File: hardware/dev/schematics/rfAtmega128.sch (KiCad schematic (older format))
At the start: 6 parts

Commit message: New schematic to finish at home.
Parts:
- added C?: 330n, symbol CAP_0603
- added C?: 22u, symbol CAP_0603
- added C? (x14): 100n, symbol CAP_0603
- added C?: 4.7u, symbol CAP_0603
- added J?: TEST_VDD33, symbol TEST_PAD
- added J?: TEST_GND, symbol TEST_PAD
- added J? (x2): J2PIN, symbol J2PIN
- added J?: PWR_ON/OFF, symbol J2PIN
- added R? (x12): RES_0603, symbol RES_0603
- added U?: FT232RL, symbol FT232RL
- added U?: LED_RED, symbol LED_RED
- added U? (x2): LED_GREEN, symbol LED_GREEN
- added U?: Q16.000, symbol Q16.000
- added XT?: FTDI_CONN, symbol FTDI_CONN
- gave numbers to parts that had none: 1
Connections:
- net GND: now reaches U?.11 (TEST)
- net GND: now also U?.1, U?.10 (AVSS_RFN), U?.20 (DVSS:DSVSS), U?.24 (DVSS), U?.35 (DVSS), U?.45 (DVSS), U?.55 (DVSS), U?.58 (AVSS:AVSS), U?.6 (GND), U?.61 (AVSS), U?.65 (AVSS_PAD), U?.7 (AVSS_RFP), XT?.4 (GND), XT?.5 (Shield), XT?.6 (Shield), C?.2, C?.2, C?.2, C?.2, C?.2, C?.2, C?.2, C?.2, C?.2, C?.2, C?.2, C?.2, C?.2, C?.2, C?.2, C?.2, J?.1, R?.2, U?.18 (GND), U?.2 (K), U?.21 (GND), U?.25 (AGND), U?.26 (TEST), U?.7 (GND), XT?.16
- net RESET: now reaches U?.12 (RESET)
- net RESET: now also C?.2, R?.1, R?.2
- net pwr_atmega: now reaches U?.33 (CLKI)
- net pwr_atmega: now also U?.21 (DVDD), U?.22 (DVDD), U?.23 (DEVDD), U?.34 (DEVDD), U?.44 (DEVDD), U?.54 (DEVDD), U?.59 (EVDD), C?.1, C?.1, C?.1, C?.1, C?.1, J?.2, R?.2
- net at U?.56 (XTAL2): now also C?.1, R?.2, U?.1
- net at U?.57 (XTAL1): now also C?.1, R?.1, U?.3
- net at U?.60 (AVDD): now also C?.1
- net aref: now reaches U?.62 (AREF)
- net aref: now also C?.1
- net at XT?.1 (VCC): now also U?.1 (A)
- net DM: now reaches XT?.2 (DM)
- net DM: now also R?.2
- net DP: now reaches XT?.3 (DP)
- net DP: now also R?.2
- net at U?.2 (K): now also U?.2 (VCC), C?.1, J?.1
- net at U?.1 (CTL): now also J?.2, R?.1
- net vdd33: now reaches U?.4 (OUT)
- net vdd33: now also C?.1, J?.1, J?.1, J?.1, R?.1
- net at U?.3: now also R?.1
- new net: R?.1, U?.15 (USBDP)
- new net: R?.1, U?.16 (USBDM)
- new net: C?.1, C?.1, U?.17 (3V3OUT), U?.4 (VCCIO)
- new net: C?.1, U?.19 (RESET#)
- new net: R?.2, U?.1 (A)
- new net: R?.1, U?.1 (A) (x2)
- new net CBUS0_CONN: U?.2 (K), U?.23 (CBUS0), XT?.11
- new net CBUS1_CONN: U?.2 (K), U?.22 (CBUS1), XT?.12
- new net CBUS2_CONN: U?.13 (CBUS2), XT?.13
- new net CBUS3_CONN: U?.14 (CBUS3), XT?.14
- new net CBUS4_CONN: U?.12 (CBUS4), XT?.15
- new net CTS_CONN: U?.11 (CTS#), XT?.6
- new net DCD_CONN: U?.10 (DCD#), XT?.9
- new net DSR_CONN: U?.9 (DSR#), XT?.8
- new net DTR_CONN: C?.1, U?.2 (DTR#), XT?.7
- new net RI_CONN: U?.6 (RI#), XT?.10
- new net RTS_CONN: R?.1, U?.3 (RTS#), XT?.5
- new net RXD: R?.2
- new net RXD_CONN: R?.1, U?.5 (RXD), XT?.4
- new net TXD: R?.2
- new net TXD_CONN: R?.1, U?.1 (TXD), XT?.3
- new net pwr_ftdi: C?.1, C?.1, J?.2, R?.2, R?.2, U?.20 (VCC)
- no-connect marks 0 -> 9
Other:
- note added: "FTDI Chip connector\nContains all FTDI pins on a 2x7 pins connector\nPins are 3.3V level internal connected"
- note added: "FTDI\nAll signals are lead to XT connector.\nRXD and TXD pins are flipped and lead to ATmega128rfA1"
- note added: "POWER SUPPLY \nInput: 4.0 - 32.0 VDC\nOutput: 3.3 VDC"
- moved on the sheet: U?, U?A, U?B, XT?

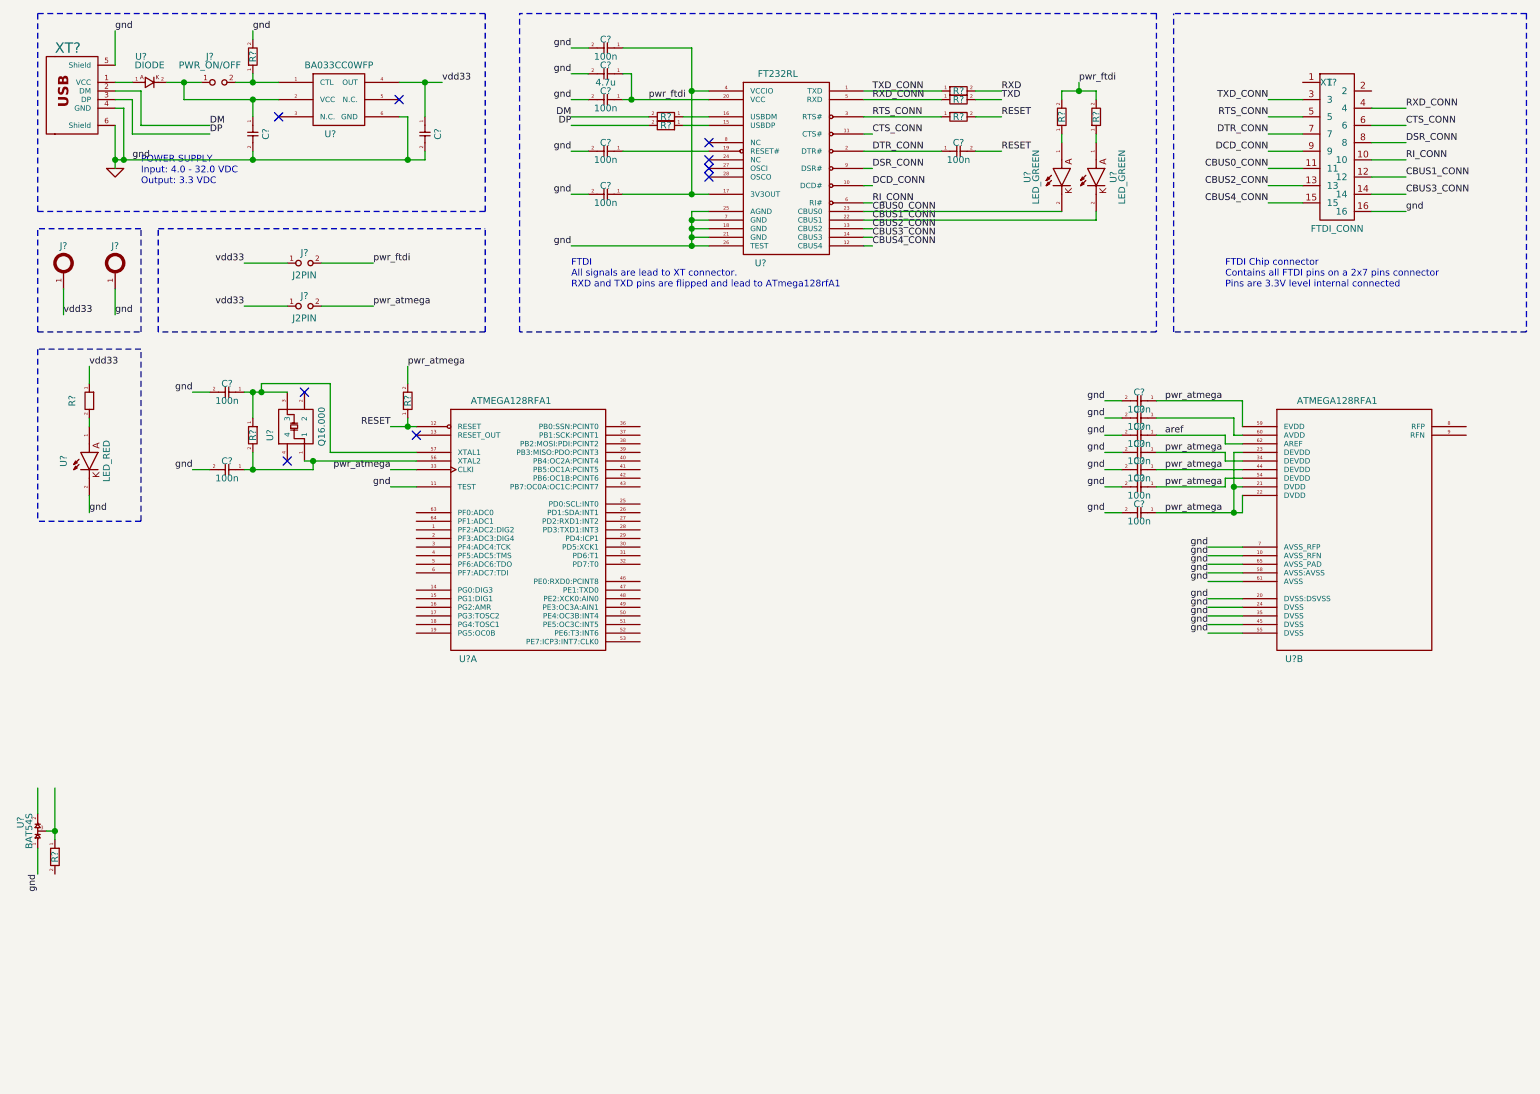
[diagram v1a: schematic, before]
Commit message: dev board schematic is finished now. Need to add modules of few resistors and condensators.
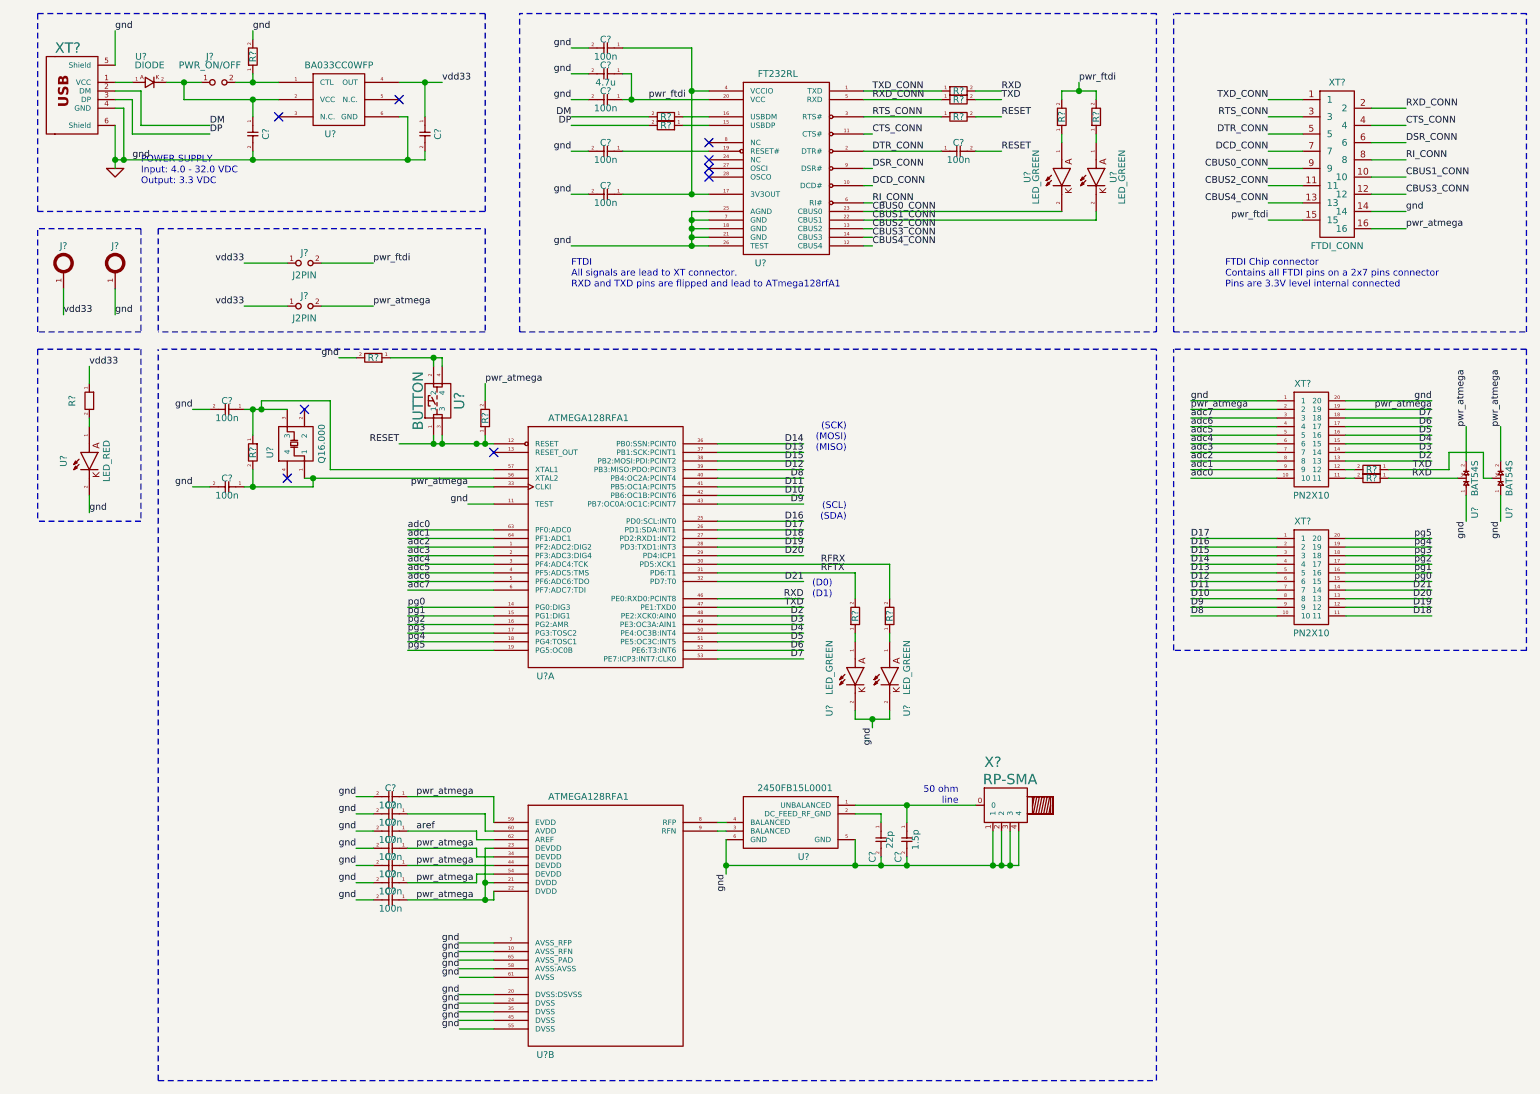
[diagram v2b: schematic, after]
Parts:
- removed R?: RES_0603, symbol RES_0603
- added C?: 22p, symbol CAP_0603
- added C?: 1.5p, symbol CAP_0603
- added R? (x4): RES_0603, symbol RES_0603
- added R?: 51, r_0603, symbol RES_0603
- added U?: BAT54S, SOT23EBC, symbol BAT54S
- added U? (x2): LED_GREEN, KP-2012ZGC, symbol LED_GREEN
- added U?: 2450FB15L0001, 2450FB15L0001, symbol 2450FB15L0001
- added U?: BUTTON, symbol BUTTON
- added X?: RP-SMA, rp-sma, symbol RP-SMA
- added XT? (x2): PN2X10, symbol PN2X10
- C? (x6): footprint (none) -> c_0603
- C? (x2): footprint (none) -> c_0805
- J? (x2): footprint (none) -> testpoint_2mm5
- R? (x3): value RES_0603 -> 2.7K; footprint (none) -> r_0603
- R? (x5): value RES_0603 -> 510; footprint (none) -> r_0603
- R?: value RES_0603 -> 100K; footprint (none) -> r_0603
- R?: footprint (none) -> r_0603
- U? (x2): footprint (none) -> atmega128rfa1
- U?: footprint (none) -> melf
- U?: footprint (none) -> BA033CCOWFP
- U?: footprint (none) -> SOT23EBC
- U?: footprint (none) -> SSOP28
- U? (x3): footprint (none) -> KP-2012ZGC
- U?: footprint (none) -> crystal_xg6x3p5
- XT?: footprint (none) -> USB_B
- XT?: footprint (none) -> BH16R
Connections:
- net CBUS0_CONN: now also XT?.9; no longer XT?.11
- net CBUS1_CONN: now also XT?.10; no longer XT?.12
- net CBUS2_CONN: now also XT?.11; no longer XT?.13
- net CBUS3_CONN: now also XT?.12; no longer XT?.14
- net CBUS4_CONN: now also XT?.13; no longer XT?.15
- net CTS_CONN: now also XT?.4; no longer XT?.6
- net DCD_CONN: now also XT?.7; no longer XT?.9
- net DSR_CONN: now also XT?.6; no longer XT?.8
- net DTR_CONN: now also XT?.5; no longer XT?.7
- net GND: now also XT?.14, C?.2, C?.2, R?.2, U?.1, U?.2 (K), U?.2 (K), U?.5 (GND), U?.6 (GND), X?.1, X?.2, X?.3, X?.4, XT?.1, XT?.20; no longer XT?.16
- net RESET: now also U?.1, U?.3
- net RI_CONN: now also XT?.8; no longer XT?.10
- net RTS_CONN: now also XT?.3; no longer XT?.5
- net RXD: now also U?.3, U?.46 (PE0:RXD0:PCINT8), R?.1
- net RXD_CONN: now also XT?.2; no longer XT?.4
- net TXD: now also U?.47 (PE1:TXD0), R?.1, U?.3
- net TXD_CONN: now also XT?.1; no longer XT?.3
- net pwr_atmega: now also U?.2, XT?.16, U?.2, XT?.19, XT?.2
- net pwr_ftdi: now also XT?.15
- net adc2: now reaches U?.1 (PF2:ADC2:DIG2)
- net adc2: now also XT?.8
- net pg0: now reaches U?.14 (PG0:DIG3)
- net pg0: now also XT?.15
- net pg1: now reaches U?.15 (PG1:DIG1)
- net pg1: now also XT?.16
- net pg2: now reaches U?.16 (PG2:AMR)
- net pg2: now also XT?.17
- net pg3: now reaches U?.17 (PG3:TOSC2)
- net pg3: now also XT?.18
- net pg4: now reaches U?.18 (PG4:TOSC1)
- net pg4: now also XT?.19
- net pg5: now reaches U?.19 (PG5:OC0B)
- net pg5: now also XT?.20
- net adc3: now reaches U?.2 (PF3:ADC3:DIG4)
- net adc3: now also XT?.7
- net D16: now reaches U?.25 (PD0:SCL:INT0)
- net D16: now also XT?.2
- net D17: now reaches U?.26 (PD1:SDA:INT1)
- net D17: now also XT?.1
- net D18: now reaches U?.27 (PD2:RXD1:INT2)
- net D18: now also XT?.11
- net D19: now reaches U?.28 (PD3:TXD1:INT3)
- net D19: now also XT?.12
- net D20: now reaches U?.29 (PD4:ICP1)
- net D20: now also XT?.13
- net adc4: now reaches U?.3 (PF4:ADC4:TCK)
- net adc4: now also XT?.6
- net RFRX: now reaches U?.30 (PD5:XCK1)
- net RFRX: now also R?.2
- net RFTX: now reaches U?.31 (PD6:T1)
- net RFTX: now also R?.2
- net D21: now reaches U?.32 (PD7:T0)
- net D21: now also XT?.14
- net D14: now reaches U?.36 (PB0:SSN:PCINT0)
- net D14: now also XT?.4
- net D13: now reaches U?.37 (PB1:SCK:PCINT1)
- net D13: now also XT?.5
- net D15: now reaches U?.38 (PB2:MOSI:PDI:PCINT2)
- net D15: now also XT?.3
- net D12: now reaches U?.39 (PB3:MISO:PDO:PCINT3)
- net D12: now also XT?.6
- net adc5: now reaches U?.4 (PF5:ADC5:TMS)
- net adc5: now also XT?.5
- net D8: now reaches U?.40 (PB4:OC2A:PCINT4)
- net D8: now also XT?.10
- net D11: now reaches U?.41 (PB5:OC1A:PCINT5)
- net D11: now also XT?.7
- net D10: now reaches U?.42 (PB6:OC1B:PCINT6)
- net D10: now also XT?.8
- net D9: now reaches U?.43 (PB7:OC0A:OC1C:PCINT7)
- net D9: now also XT?.9
- net D2: now reaches U?.48 (PE2:XCK0:AIN0)
- net D2: now also XT?.13
- net D3: now reaches U?.49 (PE3:OC3A:AIN1)
- net D3: now also XT?.14
- net adc6: now reaches U?.5 (PF6:ADC6:TDO)
- net adc6: now also XT?.4
- net D4: now reaches U?.50 (PE4:OC3B:INT4)
- net D4: now also XT?.15
- net D5: now reaches U?.51 (PE5:OC3C:INT5)
- net D5: now also XT?.16
- net D6: now reaches U?.52 (PE6:T3:INT6)
- net D6: now also XT?.17
- net D7: now reaches U?.53 (PE7:ICP3:INT7:CLK0)
- net D7: now also XT?.18
- net adc7: now reaches U?.6 (PF7:ADC7:TDI)
- net adc7: now also XT?.3
- net adc0: now reaches U?.63 (PF0:ADC0)
- net adc0: now also XT?.10
- net adc1: now reaches U?.64 (PF1:ADC1)
- net adc1: now also XT?.9
- net at U?.8 (RFP): now also U?.4 (BALANCED)
- net at U?.9 (RFN): now also U?.3 (BALANCED)
- new net: R?.2, XT?.11
- new net: R?.2, XT?.12
- new net: R?.1, U?.1 (A) (x2)
- new net: C?.1, U?.1 (UNBALANCED), X?.0
- new net: C?.1, U?.2 (DC_FEED_RF_GND)
- new net: R?.1, U?.2, U?.4
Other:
- note added: "(D0)\n(D1)"
- note added: "(SCK)\n(MOSI)\n(MISO)"
- note added: "(SCL)\n(SDA)"
- note added: "50 ohm\nline"
- moved on the sheet: C?, R?, U?, U?A, U?B, XT?

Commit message: Initial pcb board layout started.
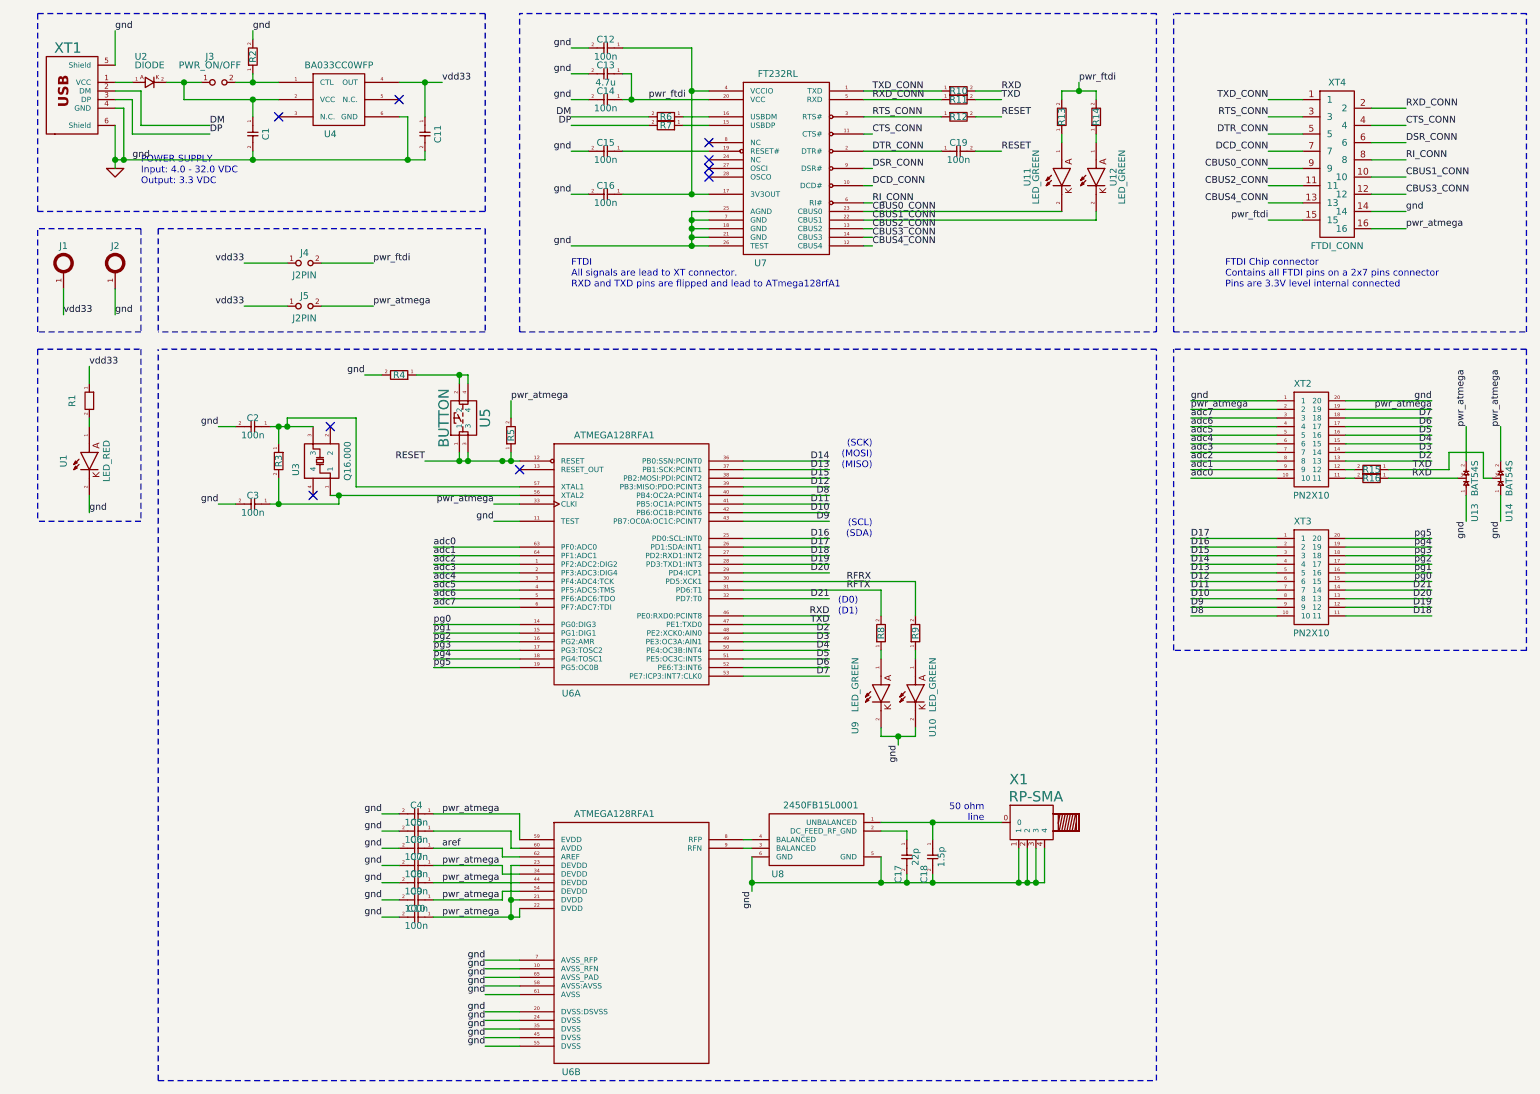
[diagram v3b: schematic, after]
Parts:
- C10, C17, C18, C2, C3, C4, C5, C6, C7, C8, C9: renamed from C?; footprint (none) -> c_0603
- J3, J4, J5: renamed from J?; footprint (none) -> JUMPER2PINS
- R15, R16, R8, R9: renamed from R?; footprint (none) -> r_0603
- R3: renamed from R?; value RES_0603 -> 1M; footprint (none) -> r_0603
- U5: renamed from U?; footprint (none) -> PCB_PUSH
- XT2, XT3: renamed from XT?; footprint (none) -> PN2X10
- gave numbers to parts that had none: 37
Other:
- moved on the sheet: C10, C17, C18, C2, C3, C4, C5, C6, C7, C8, C9, R3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
